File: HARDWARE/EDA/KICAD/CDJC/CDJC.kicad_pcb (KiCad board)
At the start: 2 copper layers, 100 x 100 mm, 63 parts, among them J1 COM_IN, J2 COM_OUT, J3 POWER_IN, J4 POWER_OUT, J5 BIT_OUT, Q1 BC549, SW1 B-SET, U1 74LS04, U2 74LS32, U3 74LS08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

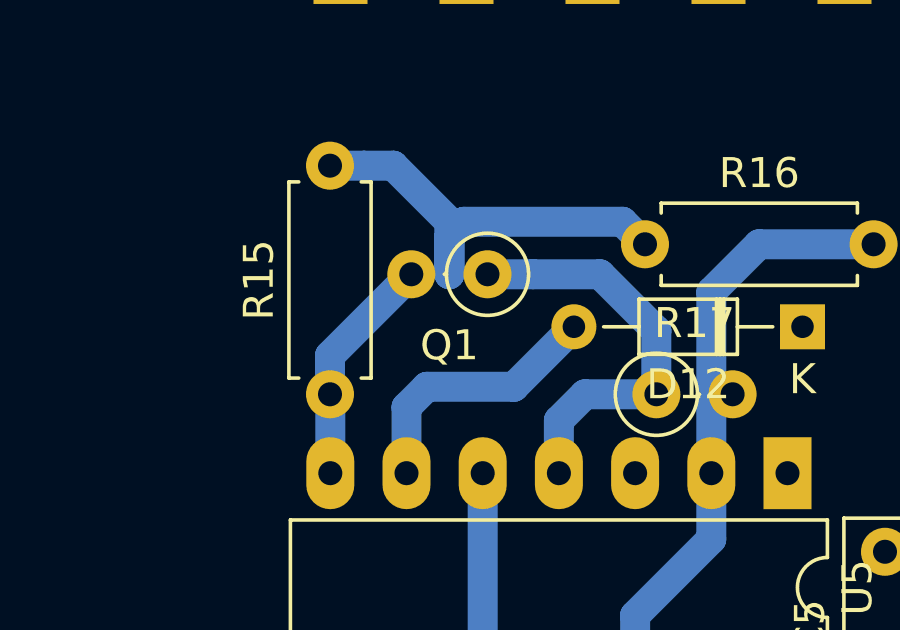
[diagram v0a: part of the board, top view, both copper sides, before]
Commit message: adjust footprint to bc 547
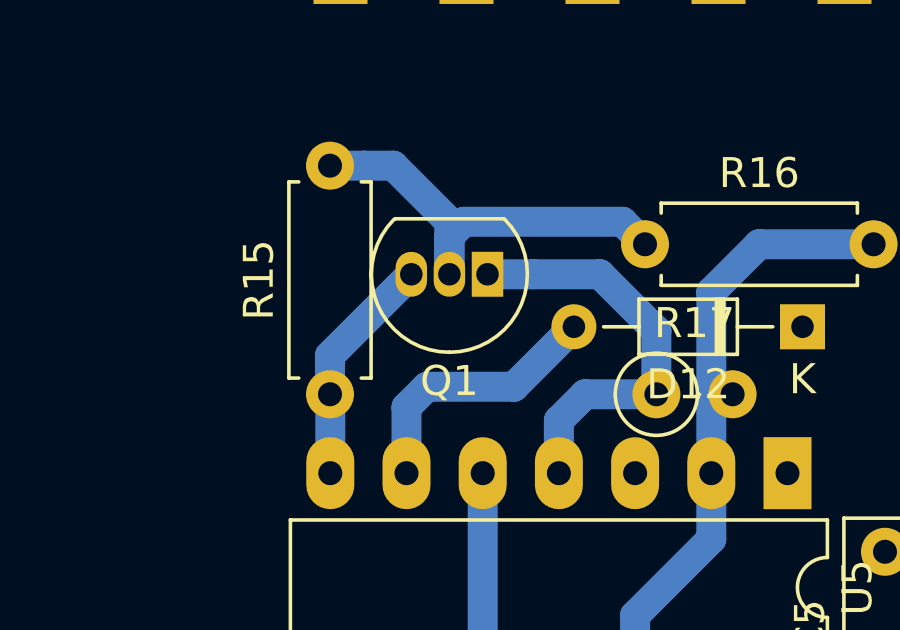
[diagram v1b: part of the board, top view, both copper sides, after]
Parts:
- Q1: footprint Resistor_THT:R_Axial_DIN0207_L6.3mm_D2.5mm_P2.54mm_Vertical -> Package_TO_SOT_THT:TO-92_Inline
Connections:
- R9 pad 1: MRI -> GNDD
- R9 pad 2: GNDD -> MRI
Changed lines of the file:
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@@
     (add_net "Net-(U9-Pad12)")
+  )
+  (module Package_TO_SOT_THT:TO-92_Inline (layer F.Cu)
+    (at 194.1 127.15 180)
+    (descr "TO-92 leads in-line, narrow, oval pads, drill 0.75mm (see NXP sot054_po.pdf)")
+    (tags "to-92 sc-43 sc-43a sot54 PA33 transistor")
+    (fp_text reference Q1 (at 1.27 -3.56) (layer F.SilkS)
+      (effects (font (size 1 1) (thickness 0.15)))
+    )
+    (fp_text value BC549 (at 1.27 2.79) (layer F.Fab)
+      (effects (font (size 1 1) (thickness 0.15)))
+    )
+    (fp_arc (start 1.27 0) (end 1.27 -2.6) (angle 135) (layer F.SilkS) (width 0.12))
+    (fp_arc (start 1.27 0) (end 1.27 -2.48) (angle -135) (layer F.Fab) (width 0.1))
+    (fp_arc (start 1.27 0) (end 1.27 -2.6) (angle -135) (layer F.SilkS) (width 0.12))
+    (fp_arc (start 1.27 0) (end 1.27 -2.48) (angle 135) (layer F.Fab) (width 0.1))
+    (fp_text user %R (at 1.27 0) (layer F.Fab)
+      (effects (font (size 1 1) (thickness 0.15)))
+    )
+    (fp_line (start -0.53 1.85) (end 3.07 1.85) (layer F.SilkS) (width 0.12))
+    (fp_line (start -0.5 1.75) (end 3 1.75) (layer F.Fab) (width 0.1))
+    (fp_line (start -1.46 -2.73) (end 4 -2.73) (layer F.CrtYd) (width 0.05))
+    (fp_line (start -1.46 -2.73) (end -1.46 2.01) (layer F.CrtYd) (width 0.05))
+    (fp_line (start 4 2.01) (end 4 -2.73) (layer F.CrtYd) (width 0.05))
+    (fp_line (start 4 2.01) (end -1.46 2.01) (layer F.CrtYd) (width 0.05))
+    (pad 1 thru_hole rect (at 0 0 180) (size 1.05 1.5) (drill 0.75) (layers *.Cu *.Mask)
+      (net 39 "Net-(Q1-Pad1)"))
+    (pad 3 thru_hole oval (at 2.54 0 180) (size 1.05 1.5) (drill 0.75) (layers *.Cu *.Mask)
+      (net 1 GNDD))
+    (pad 2 thru_hole oval (at 1.27 0 180) (size 1.05 1.5) (drill 0.75) (layers *.Cu *.Mask)
+      (net 40 "Net-(Q1-Pad2)"))
+    (model ${KISYS3DMOD}/Package_TO_SOT_THT.3dshapes/TO-92_Inline.wrl
+      (at (xyz 0 0 0))
+      (scale (xyz 1 1 1))
+      (rotate (xyz 0 0 0))
+    )
   )
   (module Resistor_THT:R_Axial_DIN0207_L6.3mm_D2.5mm_P2.54mm_Vertical (layer F.Cu)
@@
       (net 2 +5VD))
     (pad 1 thru_hole circle (at 0 0) (size 1.6 1.6) (drill 0.8) (layers *.Cu *.Mask)
-      (net 39 "Net-(Q1-Pad1)"))
-    (model ${KISYS3DMOD}/Resistor_THT.3dshapes/R_Axial_DIN0207_L6.3mm_D2.5mm_P2.54mm_Vertical.wrl
-      (at (xyz 0 0 0))
-      (scale (xyz 1 1 1))
-      (rotate (xyz 0 0 0))
-    )
-  )
-  (module Resistor_THT:R_Axial_DIN0207_L6.3mm_D2.5mm_P2.54mm_Vertical (layer F.Cu)
-    (at 194.1 127.15 180)
-    (descr "Resistor, Axial_DIN0207 series, Axial, Vertical, pin pitch=2.54mm, 0.25W = 1/4W, length*diameter=6.3*2.5mm^2, http://cdn-reichelt.de/documents/datenblatt/B400/1_4W%23YAG.pdf")
-    (tags "Resistor Axial_DIN0207 series Axial Vertical pin pitch 2.54mm 0.25W = 1/4W length 6.3mm diameter 2.5mm")
-    (fp_text reference Q1 (at 1.27 -2.37) (layer F.SilkS)
-      (effects (font (size 1 1) (thickness 0.15)))
-    )
-    (fp_text value BC549 (at 1.27 2.37) (layer F.Fab)
-      (effects (font (size 1 1) (thickness 0.15)))
-    )
-    (fp_text user %R (at 1.27 -2.37) (layer F.Fab)
-      (effects (font (size 1 1) (thickness 0.15)))
-    )
-    (fp_circle (center 0 0) (end 1.25 0) (layer F.Fab) (width 0.1))
-    (fp_circle (center 0 0) (end 1.37 0) (layer F.SilkS) (width 0.12))
-    (fp_line (start 0 0) (end 2.54 0) (layer F.Fab) (width 0.1))
-    (fp_line (start 1.37 0) (end 1.44 0) (layer F.SilkS) (width 0.12))
-    (fp_line (start -1.5 -1.5) (end -1.5 1.5) (layer F.CrtYd) (width 0.05))
-    (fp_line (start -1.5 1.5) (end 3.59 1.5) (layer F.CrtYd) (width 0.05))
-    (fp_line (start 3.59 1.5) (end 3.59 -1.5) (layer F.CrtYd) (width 0.05))
-    (fp_line (start 3.59 -1.5) (end -1.5 -1.5) (layer F.CrtYd) (width 0.05))
-    (pad 2 thru_hole oval (at 2.54 0 180) (size 1.6 1.6) (drill 0.8) (layers *.Cu *.Mask)
-      (net 40 "Net-(Q1-Pad2)"))
-    (pad 1 thru_hole circle (at 0 0 180) (size 1.6 1.6) (drill 0.8) (layers *.Cu *.Mask)
       (net 39 "Net-(Q1-Pad1)"))
     (model ${KISYS3DMOD}/Resistor_THT.3dshapes/R_Axial_DIN0207_L6.3mm_D2.5mm_P2.54mm_Vertical.wrl
@@
     )
     (pad 2 thru_hole oval (at 2.54 0 180) (size 1.6 1.6) (drill 0.8) (layers *.Cu *.Mask)
+      (net 36 MRI))
+    (pad 1 thru_hole circle (at 0 0 180) (size 1.6 1.6) (drill 0.8) (layers *.Cu *.Mask)
       (net 1 GNDD))
-    (pad 1 thru_hole circle (at 0 0 180) (size 1.6 1.6) (drill 0.8) (layers *.Cu *.Mask)
-      (net 36 MRI))
     (model ${KISYS3DMOD}/Resistor_THT.3dshapes/R_Axial_DIN0207_L6.3mm_D2.5mm_P2.54mm_Vertical.wrl
       (at (xyz 0 0 0))

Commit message: stop work, go home
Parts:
- D20, D21, D9: footprint Diode_THT:D_DO-34_SOD68_P7.62mm_Horizontal -> Diode_THT:D_DO-34_SOD68_P2.54mm_Vertical_AnodeUp
- R15, R16: footprint Resistor_THT:R_Axial_DIN0207_L6.3mm_D2.5mm_P7.62mm_Horizontal -> Resistor_THT:R_Axial_DIN0207_L6.3mm_D2.5mm_P2.54mm_Vertical
- R17: footprint Resistor_THT:R_Axial_DIN0207_L6.3mm_D2.5mm_P2.54mm_Vertical -> Resistor_THT:R_Axial_DIN0207_L6.3mm_D2.5mm_P7.62mm_Horizontal
- moved C7 104.8 mm to (131.4, 114.2), turned to 0 degrees
- moved U4 78.3 mm to (187.9, 59.3), turned to 90 degrees
- moved C5 78.2 mm to (129.3, 136.3), turned to 180 degrees
- moved C2 61.9 mm to (114.3, 44.3), turned to 90 degrees
- moved C9 58.5 mm to (130.7, 78.9), turned to 90 degrees
- moved U1 54.8 mm to (203.2, 66.1), turned to 270 degrees
- moved U3 49.7 mm to (215.3, 50.4)
- moved C3 46.5 mm to (131.3, 107.2), turned to 0 degrees
- moved C8 45.8 mm to (129.2, 126.8)
- moved U2 45.7 mm to (168.1, 52.8)
- moved R7 45.2 mm to (177.7, 140.1), turned to 180 degrees
- moved U9 45.0 mm to (186.2, 108.2), turned to 90 degrees
- moved D3 44.7 mm to (166.3, 76.6), turned to 0 degrees
- moved C4 43.1 mm to (131.8, 63.3), turned to 270 degrees
- moved C6 43.1 mm to (135.5, 97.7)
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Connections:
- R9 pad 1: GNDD -> MRI
- R9 pad 2: MRI -> GNDD
- U6 pad 12: MRLMon -> Net-(D10-Pad1)
- U6 pad 13: Net-(D10-Pad1) -> MRLMon
- U6 pad 4: Net-(U6-Pad2) -> MRI
- U6 pad 5: MRI -> Net-(U6-Pad2)
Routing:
- net CLK: track 19.7 -> 97.1 mm
- net GNDD: track 117.6 -> 144.7 mm
- net LBLBI: track 19.7 -> 46.6 mm
- net EI: track 19.7 -> 46.0 mm
- net MRI: track 19.7 -> 42.7 mm
- net +5VD: track 51.1 -> 39.2 mm
- net Net-(U6-Pad2): track 0.00 -> 11.3 mm
- net Net-(D10-Pad1): track 20.8 -> 28.0 mm
- net Net-(Q1-Pad2): track 14.8 -> 8.83 mm
- net Net-(D12-Pad2): track 8.89 -> 3.03 mm
- net Net-(Q1-Pad1): track 13.9 -> 10.00 mm
- net Net-(D21-Pad1): track 2.77 -> 0.07 mm
- net Net-(D7-Pad2): track 0.00 -> 2.29 mm
- net Net-(D8-Pad2): track 0.00 -> 2.28 mm
- net Net-(D6-Pad2): track 0.00 -> 2.28 mm
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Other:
- outline, holes or cut-outs redrawn

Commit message: pause work for sleep
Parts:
- removed C2, C3, C4, C5, C6, C7, C8, C9: 100nF 63V, Capacitor_THT:C_Rect_L7.0mm_W2.5mm_P5.00mm
- R11, R8, R9: footprint Resistor_THT:R_Axial_DIN0207_L6.3mm_D2.5mm_P2.54mm_Vertical -> Resistor_THT:R_Axial_DIN0207_L6.3mm_D2.5mm_P7.62mm_Horizontal
- moved C10 104.0 mm to (229.0, 54.0), turned to 270 degrees
- moved U1 55.9 mm to (150.0, 83.2), turned to 90 degrees
- moved R3 53.3 mm to (231.9, 79.6), turned to 270 degrees
- moved U3 50.0 mm to (177.7, 83.2), turned to 90 degrees
- moved U2 46.7 mm to (203.4, 83.3), turned to 90 degrees
- moved U4 38.1 mm to (149.9, 62.4)
- moved U6 33.5 mm to (203.2, 62.5), turned to 90 degrees
- moved U8 29.0 mm to (177.7, 62.5), turned to 90 degrees
- moved R1 20.6 mm to (156.6, 98.0)
- moved R2 20.6 mm to (156.6, 93.2)
- moved R4 20.6 mm to (158.7, 100.4)
- moved R6 20.6 mm to (158.7, 90.8)
- moved R5 20.6 mm to (158.7, 95.6)
- moved D1 20.6 mm to (151.2, 99.7)
- moved D3 20.6 mm to (151.2, 90.5)
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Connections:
- J1 pad 2: CLK -> LBLBI
- J1 pad 3: LBLBI -> MRI
- J1 pad 4: MRI -> EI
- J1 pad 5: EI -> CLK
- J2 pad 2: CLK -> LBLBO
- J2 pad 3: LBLBO -> FBO
- J2 pad 4: FBO -> !LBO
- J2 pad 5: !LBO -> CLK
- U1 pad 1: FB_SW -> Net-(U1-Pad1)
- U1 pad 11: Net-(U1-Pad11) -> FB_SW
- U1 pad 13: Net-(U1-Pad13) -> NB_SW
- U1 pad 3: NB_SW -> Net-(U1-Pad3)
- U1 pad 5: LB_SW -> Net-(U1-Pad5)
- U1 pad 9: Net-(U1-Pad9) -> LB_SW
- U2 pad 11: Net-(U1-Pad9) -> Net-(U1-Pad1)
- U2 pad 6: Net-(U1-Pad13) -> Net-(U1-Pad3)
- U2 pad 8: Net-(U1-Pad11) -> Net-(U1-Pad5)
- U3 pad 1: Net-(U1-Pad12) -> GNDD
- U3 pad 10: LB_SW -> FB_SW
- U3 pad 11: Net-(U3-Pad11) -> LBMon
- U3 pad 12: GNDD -> LB_SW
- U3 pad 13: GNDD -> Net-(U1-Pad2)
- U3 pad 2: FB_SW -> GNDD
- U3 pad 3: FBMon -> Net-(U3-Pad3)
- U3 pad 4: Net-(U1-Pad10) -> Net-(U1-Pad6)
- U3 pad 8: LBMon -> FBMon
- U3 pad 9: Net-(U1-Pad8) -> Net-(U1-Pad4)
- U4 pad 1: Net-(U1-Pad2) -> FB_SW
- U4 pad 10: NB_SW -> Net-(U1-Pad8)
- U4 pad 2: Net-(U1-Pad4) -> NB_SW
- U4 pad 3: Net-(U4-Pad3) -> Net-(U4-Pad12)
- U4 pad 4: Net-(U4-Pad3) -> Net-(U1-Pad12)
- U4 pad 5: Net-(U1-Pad6) -> Net-(U1-Pad10)
- U4 pad 6: ELMon -> Net-(U4-Pad6)
- U4 pad 8: Net-(U4-Pad12) -> ELMon
- U4 pad 9: FB_SW -> Net-(U4-Pad6)
- U6 pad 1: EI -> Net-(D10-Pad1)
- U6 pad 10: FBMon -> MRI
- U6 pad 12: Net-(D10-Pad1) -> LBLBI
- U6 pad 13: MRLMon -> FBMon
- U6 pad 2: Net-(U6-Pad2) -> MRLMon
- U6 pad 4: MRI -> Net-(U6-Pad4)
- U6 pad 5: Net-(U6-Pad2) -> EI
- U6 pad 9: LBLBI -> Net-(U6-Pad4)
- U8 pad 1: Net-(U6-Pad3) -> NBMon
- U8 pad 10: LBMon -> Net-(U6-Pad8)
- U8 pad 12: Net-(U6-Pad6) -> Net-(U8-Pad12)
- U8 pad 13: Net-(U6-Pad8) -> Net-(U6-Pad3)
- U8 pad 2: Net-(U5-Pad3) -> LBMon
- U8 pad 3: Net-(U8-Pad3) -> Net-(U6-Pad4)
- U8 pad 4: Net-(U8-Pad11) -> Net-(U6-Pad6)
- U8 pad 5: Net-(U6-Pad11) -> Net-(U5-Pad3)
- U8 pad 8: Net-(U6-Pad2) -> Net-(U8-Pad12)
- U8 pad 9: NBMon -> Net-(U6-Pad11)
- U9 pad 13: Net-(U8-Pad3) -> Net-(U8-Pad6)
- U9 pad 15: Net-(U8-Pad6) -> Net-(U8-Pad11)
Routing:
- net LB_SW: track 13.5 -> 84.3 mm
- net MRLMon: track 0.00 -> 68.3 mm, vias 0 -> 4
- net FB_SW: track 31.2 -> 95.6 mm, vias 0 -> 4
- net +5VD: track 39.2 -> 91.0 mm
- net Net-(U6-Pad4): track 0.00 -> 47.2 mm
- net Net-(U1-Pad8): track 0.00 -> 38.6 mm
- net Net-(U6-Pad6): track 0.00 -> 37.8 mm, vias 0 -> 2
- net Net-(U1-Pad4): track 0.00 -> 37.7 mm
- net FBMon: track 0.00 -> 36.7 mm, vias 0 -> 4
- net Net-(U6-Pad8): track 0.11 -> 36.7 mm, vias 0 -> 2
- net Net-(U1-Pad2): track 0.00 -> 35.2 mm
- net Net-(U6-Pad3): track 0.00 -> 33.6 mm
- net GNDD: track 144.7 -> 117.8 mm, vias 0 -> 2
- net Net-(U6-Pad11): track 0.00 -> 24.1 mm
- net LBMon: track 1.04 -> 16.3 mm
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
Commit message: adjusting PCB
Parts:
- moved R3 14.3 mm to (219.4, 72.7), turned to 180 degrees
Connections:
- U2 pad 1: GNDD -> NB_SW
- U2 pad 11: Net-(U1-Pad1) -> Net-(U2-Pad11)
- U2 pad 12: FB_SW -> GNDD
- U2 pad 13: NB_SW -> GNDD
- U2 pad 2: GNDD -> LB_SW
- U2 pad 3: Net-(U2-Pad3) -> Net-(U1-Pad3)
- U2 pad 4: NB_SW -> FB_SW
- U2 pad 5: LB_SW -> NB_SW
- U2 pad 6: Net-(U1-Pad3) -> Net-(U1-Pad1)
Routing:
- net GNDD: track 117.8 -> 348.4 mm, vias 2 -> 17
- net NB_SW: track 32.6 -> 164.5 mm, vias 0 -> 8
- net LB_SW: track 84.3 -> 198.0 mm, vias 0 -> 6
- net +5VD: track 91.0 -> 181.7 mm, vias 0 -> 8
- net FB_SW: track 95.6 -> 178.4 mm, vias 4 -> 10
- net Net-(U1-Pad5): track 0.00 -> 78.9 mm, vias 0 -> 2
- net Net-(U1-Pad1): track 0.00 -> 71.8 mm
- net Net-(U1-Pad3): track 0.00 -> 66.4 mm, vias 0 -> 4
- net NBMon: track 0.00 -> 44.5 mm, vias 0 -> 2
- net Net-(U1-Pad6): track 0.00 -> 26.5 mm
- net Net-(D10-Pad1): track 23.4 -> 26.0 mm, vias 0 -> 1
- net Net-(U1-Pad2): track 35.2 -> 37.4 mm
- net FBMon: track 36.7 -> 38.0 mm
- net MRI: track 53.7 -> 52.5 mm
- net LBLBI: track 57.5 -> 56.4 mm
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
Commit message: sleep
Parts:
- moved D2 13.5 mm to (147.8, 108.2)
- moved R5 13.5 mm to (155.3, 108.7)
- moved D1 13.5 mm to (147.8, 112.7)
- moved D3 13.5 mm to (147.8, 103.6)
- moved R1 13.5 mm to (153.2, 111.1)
- moved R2 13.5 mm to (153.2, 106.3)
- moved R4 13.5 mm to (155.3, 113.5)
- moved R6 13.5 mm to (155.3, 103.9)
- moved SW1 11.9 mm to (149.1, 99.6)
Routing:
- net GNDD: track 348.4 -> 268.4 mm, vias 17 -> 12
- net Net-(U1-Pad5): track 78.9 -> 23.1 mm, vias 2 -> 1
- net Net-(U1-Pad3): track 66.4 -> 27.7 mm, vias 4 -> 2
- net FB_SW: track 178.4 -> 151.5 mm
- net LB_SW: track 198.0 -> 176.9 mm, vias 6 -> 4
- net NB_SW: track 164.5 -> 145.5 mm, vias 8 -> 6
- net +5VD: track 181.7 -> 176.6 mm

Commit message: i am crazy
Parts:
- moved R16 10.4 mm to (204.3, 137.7)
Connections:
- U2 pad 1: NB_SW -> GNDD
- U2 pad 11: Net-(U2-Pad11) -> Net-(U1-Pad3)
- U2 pad 12: GNDD -> NB_SW
- U2 pad 13: GNDD -> LB_SW
- U2 pad 2: LB_SW -> GNDD
- U2 pad 3: Net-(U1-Pad3) -> Net-(U2-Pad3)
- U2 pad 4: FB_SW -> NB_SW
- U2 pad 5: NB_SW -> FB_SW
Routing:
- net Net-(U1-Pad1): track 71.8 -> 0.00 mm
- net NB_SW: track 145.5 -> 101.1 mm, vias 6 -> 2
- net FB_SW: track 151.5 -> 114.9 mm, vias 10 -> 6
- net Net-(U1-Pad3): track 27.7 -> 0.00 mm, vias 2 -> 0
- net Net-(U1-Pad5): track 23.1 -> 3.27 mm, vias 1 -> 0
- net Net-(D10-Pad1): track 26.0 -> 17.1 mm
- net LB_SW: track 176.9 -> 169.6 mm, vias 4 -> 6
- net Net-(Q1-Pad2): track 8.46 -> 13.2 mm
- net GNDD: track 268.4 -> 265.5 mm
- net EI: track 46.7 -> 45.7 mm

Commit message: adjusting PCB
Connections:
- D9 pad 1: LBLBO -> LBLBI
- J1 pad 2: LBLBI -> MRI
- J1 pad 3: MRI -> EI
- J1 pad 4: EI -> LBLBI
- J2 pad 2: LBLBO -> FBO
- J2 pad 3: FBO -> !LBO
- J2 pad 4: !LBO -> LBLBI
- R11 pad 1: LBLBI -> MRI
- R8 pad 1: EI -> LBLBI
- R9 pad 1: MRI -> EI
- U6 pad 10: MRI -> Net-(U6-Pad10)
- U6 pad 12: LBLBI -> Net-(U6-Pad10)
- U6 pad 13: FBMon -> MRI
- U6 pad 4: Net-(U6-Pad4) -> FBMon
- U6 pad 5: EI -> LBLBI
- U6 pad 9: Net-(U6-Pad4) -> EI
- U8 pad 10: Net-(U6-Pad8) -> Net-(U6-Pad11)
- U8 pad 3: Net-(U6-Pad4) -> Net-(U6-Pad10)
- U8 pad 4: Net-(U6-Pad6) -> Net-(U6-Pad8)
- U8 pad 9: Net-(U6-Pad11) -> Net-(U6-Pad6)
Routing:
- net MRLMon: track 68.4 -> 0.00 mm, vias 4 -> 0
- net LBLBI: track 56.4 -> 119.1 mm
- net Net-(U6-Pad4): track 47.1 -> 0.00 mm
- net Net-(U6-Pad6): track 38.7 -> 0.07 mm, vias 2 -> 0
- net FBMon: track 38.0 -> 0.00 mm, vias 4 -> 0
- net Net-(U6-Pad8): track 36.1 -> 0.00 mm, vias 2 -> 0
- net Net-(U6-Pad3): track 33.6 -> 0.00 mm
- net GNDD: track 265.5 -> 241.2 mm, vias 12 -> 9
- net Net-(U6-Pad11): track 23.6 -> 0.00 mm
- net Net-(U6-Pad10): track 0.00 -> 8.49 mm
- net MRI: track 52.5 -> 59.0 mm
- net EI: track 45.7 -> 50.7 mm
- net +5VD: track 176.6 -> 172.8 mm, vias 8 -> 6
- net Net-(U1-Pad5): track 3.27 -> 0.06 mm
- net Net-(D10-Pad1): track 17.1 -> 14.5 mm, vias 1 -> 0
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
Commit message: pause work
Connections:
- U8 pad 1: NBMon -> Net-(U8-Pad1)
- U8 pad 10: Net-(U6-Pad11) -> LBMon
- U8 pad 11: Net-(U8-Pad11) -> Net-(U8-Pad1)
- U8 pad 12: Net-(U8-Pad12) -> Net-(U6-Pad6)
- U8 pad 13: Net-(U6-Pad3) -> Net-(U6-Pad11)
- U8 pad 2: LBMon -> Net-(U6-Pad3)
- U8 pad 3: Net-(U6-Pad10) -> Net-(U8-Pad3)
- U8 pad 8: Net-(U8-Pad12) -> Net-(U6-Pad10)
- U8 pad 9: Net-(U6-Pad6) -> NBMon
- U9 pad 15: Net-(U8-Pad11) -> Net-(U8-Pad3)
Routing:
- net Net-(U6-Pad6): track 0.07 -> 45.4 mm
- net NBMon: track 44.5 -> 0.00 mm, vias 2 -> 0
- net Net-(U6-Pad11): track 0.00 -> 41.9 mm
- net Net-(U6-Pad8): track 0.00 -> 39.7 mm, vias 0 -> 2
- net FB_SW: track 114.9 -> 77.1 mm, vias 6 -> 2
- net GNDD: track 241.2 -> 213.6 mm, vias 9 -> 5
- net NB_SW: track 101.1 -> 80.5 mm
- net Net-(U6-Pad10): track 8.49 -> 26.8 mm, vias 0 -> 2
- net LBMon: track 16.3 -> 1.04 mm
- net Net-(U8-Pad12): track 13.7 -> 0.00 mm
- net Net-(U8-Pad1): track 0.00 -> 13.4 mm
- net LB_SW: track 171.4 -> 167.6 mm, vias 6 -> 2
- net LBLBI: track 119.1 -> 116.8 mm
- net +5VD: track 172.8 -> 174.2 mm
